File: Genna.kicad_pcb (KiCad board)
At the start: 2 copper layers, 12 x 17.8 mm, 14 parts, among them J1 USB_A, J2 Conn_01x09, J3 Conn_01x09, U1 ATmega32U4-M

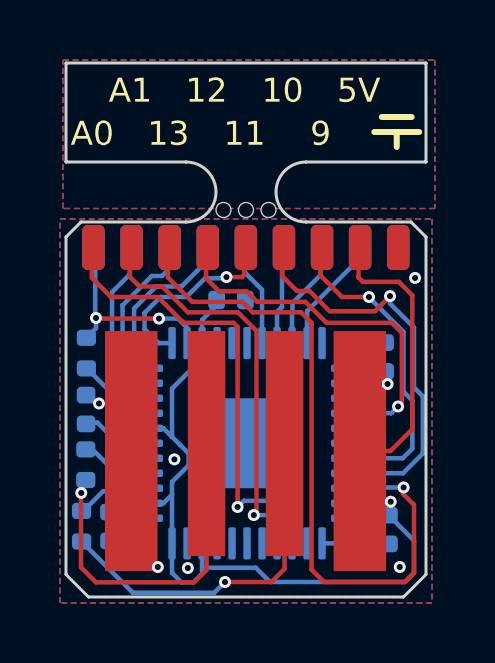
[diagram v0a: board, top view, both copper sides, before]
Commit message: changed via dimensions and had to remove an IO
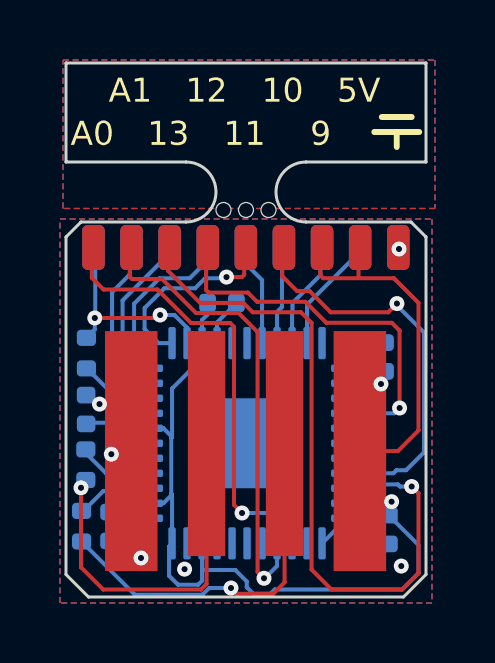
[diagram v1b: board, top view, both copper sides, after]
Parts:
- moved C5 0.32 mm to (133.6, 76.7)
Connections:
- J3 pad 3: 9 -> +5V
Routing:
- net 9: track 10.8 -> 0.00 mm, vias 1 -> 0
- net +5V: track 42.7 -> 46.4 mm
- net A1: track 13.7 -> 15.6 mm
- net GND: track 2.49 -> 4.10 mm
- net Net-(J1-Pad3): track 11.3 -> 11.9 mm
- net 13: track 23.4 -> 24.0 mm
